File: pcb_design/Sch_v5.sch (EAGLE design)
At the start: 32 parts

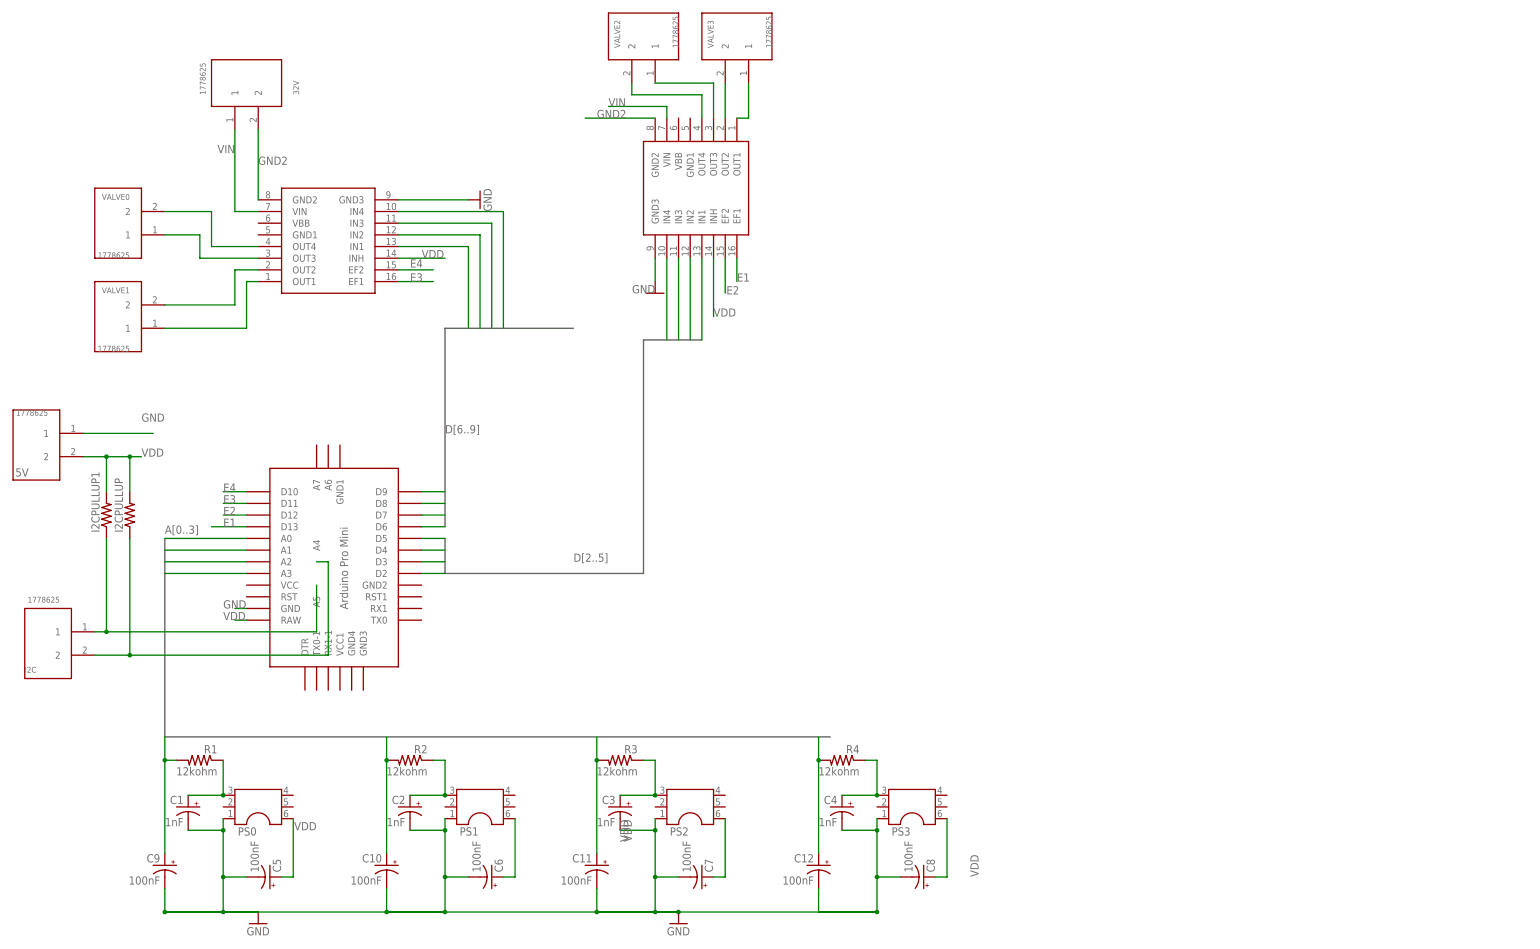
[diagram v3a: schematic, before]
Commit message: added byu parts library
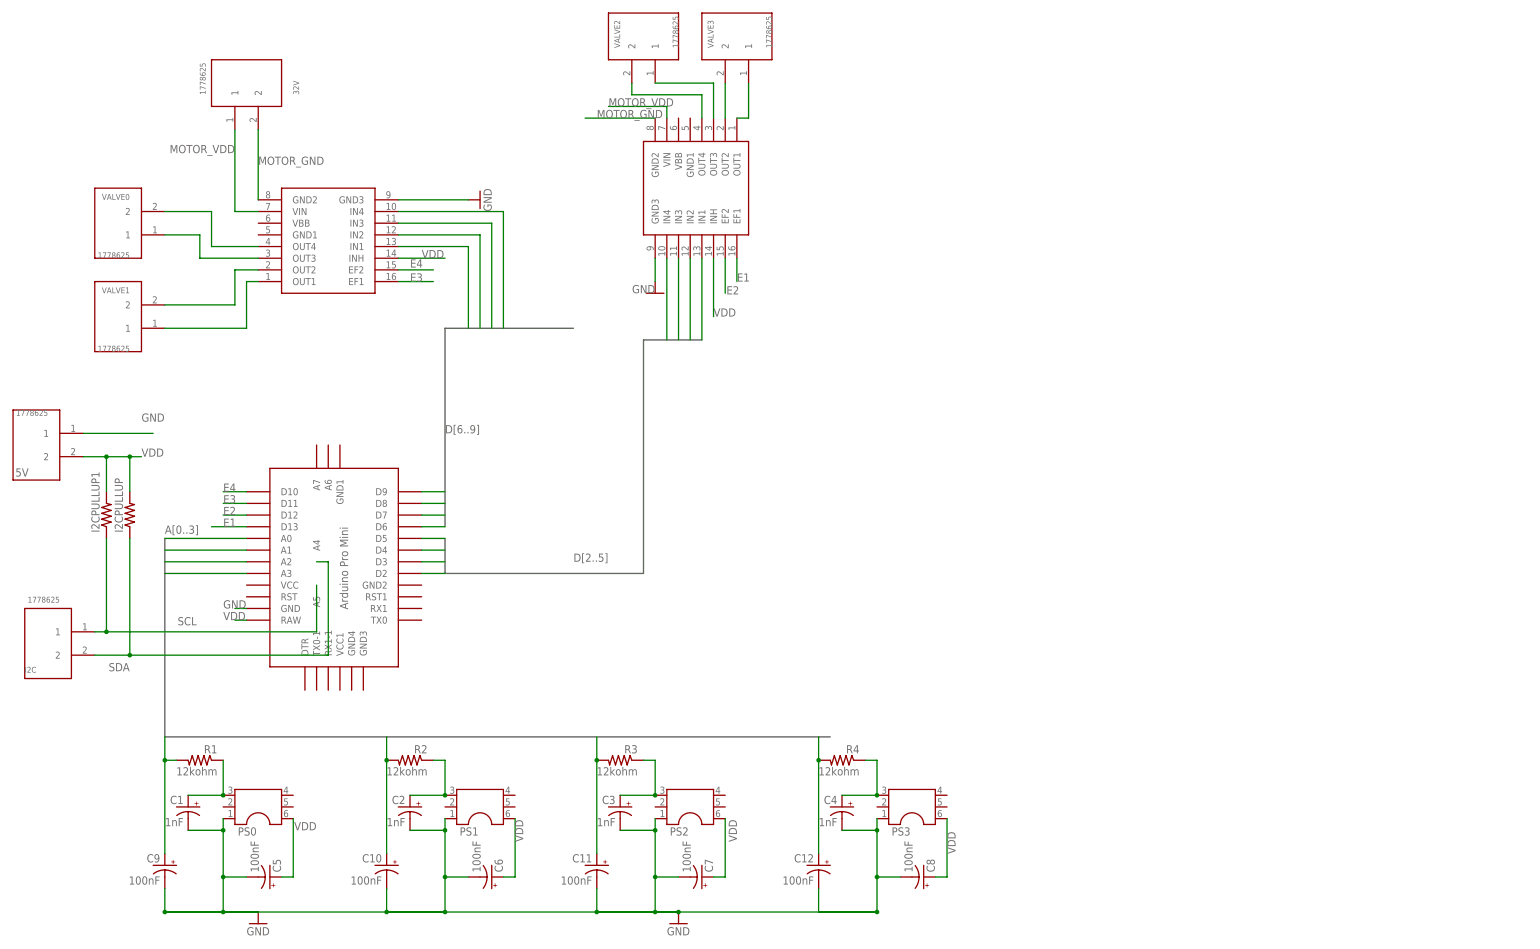
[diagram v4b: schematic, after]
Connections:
- net GND2 renamed MOTOR_GND
- net N$21 renamed SCL
- net N$9 renamed SDA
- net VIN renamed MOTOR_VDD
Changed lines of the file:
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@@
 <setting verticaltext="up"/>
 </settings>
-<grid distance="0.1" unitdist="inch" unit="inch" style="lines" multiple="1" display="no" altdistance="0.01" altunitdist="inch" altunit="inch"/>
+<grid distance="5" unitdist="mm" unit="mm" style="lines" multiple="1" display="no" altdistance="0.01" altunitdist="inch" altunit="inch"/>
 <layers>
 <layer number="1" name="Top" color="4" fill="1" visible="no" active="no"/>
@@
 </class>
 <class number="1" name="Power" width="0.3048" drill="0">
+<clearance class="1" value="0.508"/>
 </class>
-<class number="2" name="GND" width="0" drill="0">
+<class number="2" name="Motor Power" width="0.3048" drill="0">
+<clearance class="2" value="1.27"/>
 </class>
-<class number="3" name="Motor Power" width="0.3048" drill="0">
-<clearance class="3" value="0.0508"/>
+<class number="3" name="Analog Signal" width="0" drill="0">
+<clearance class="3" value="0.254"/>
+</class>
+<class number="4" name="I2C Bus" width="0" drill="0">
 </class>
 </classes>
@@
 </busses>
 <nets>
-<net name="GND" class="3">
+<net name="GND" class="0">
 <segment>
 <pinref part="GND4" gate="1" pin="GND"/>
@@
 <wire x1="58.42" y1="27.94" x2="58.42" y2="15.24" width="0.1524" layer="91"/>
 <wire x1="58.42" y1="15.24" x2="55.88" y2="15.24" width="0.1524" layer="91"/>
-<label x="81.28" y="22.86" size="1.778" layer="95" rot="MR90"/>
+<label x="58.42" y="22.86" size="1.778" layer="95" rot="MR90"/>
 </segment>
 <segment>
@@
 <wire x1="104.14" y1="27.94" x2="104.14" y2="15.24" width="0.1524" layer="91"/>
 <wire x1="104.14" y1="15.24" x2="101.6" y2="15.24" width="0.1524" layer="91"/>
-<label x="83.82" y="22.86" size="1.778" layer="95" rot="R90"/>
+<label x="106.68" y="22.86" size="1.778" layer="95" rot="R90"/>
 </segment>
 <segment>
@@
 <wire x1="152.4" y1="27.94" x2="152.4" y2="15.24" width="0.1524" layer="91"/>
 <wire x1="152.4" y1="15.24" x2="149.86" y2="15.24" width="0.1524" layer="91"/>
-<label x="157.48" y="15.24" size="1.778" layer="95" rot="MR90"/>
+<label x="152.48" y="20.24" size="1.778" layer="95" rot="MR90"/>
 </segment>
 <segment>
@@
 </segment>
 </net>
-<net name="VIN" class="3">
+<net name="MOTOR_VDD" class="2">
 <segment>
 <pinref part="U$3" gate="G$1" pin="VIN"/>
@@
 </segment>
 </net>
-<net name="GND2" class="0">
+<net name="MOTOR_GND" class="0">
 <segment>
 <pinref part="U$3" gate="G$1" pin="GND2"/>
@@
 </segment>
 </net>
-<net name="N$21" class="0">
+<net name="SCL" class="4">
 <segment>
 <pinref part="U$1" gate="G$1" pin="A5"/>
@@
 <junction x="-30.48" y="68.58"/>
 <pinref part="I2CPULLUP1" gate="G$1" pin="1"/>
+<label x="-15" y="70" size="1.778" layer="95"/>
 </segment>
 </net>
@@
 </segment>
 </net>
-<net name="A0" class="0">
+<net name="A0" class="3">
 <segment>
 <pinref part="U$1" gate="G$1" pin="A0"/>
@@
 </segment>
 </net>
-<net name="A1" class="0">
+<net name="A1" class="3">
 <segment>
 <pinref part="U$1" gate="G$1" pin="A1"/>
@@
 </segment>
 </net>
-<net name="A2" class="0">
+<net name="A2" class="3">
 <segment>
 <pinref part="U$1" gate="G$1" pin="A2"/>
@@
 </segment>
 </net>
-<net name="A3" class="0">
+<net name="A3" class="3">
 <segment>
 <pinref part="U$1" gate="G$1" pin="A3"/>
@@
 </segment>
 </net>
-<net name="N$9" class="0">
+<net name="SDA" class="4">
 <segment>
 <pinref part="I2C" gate="G$1" pin="2"/>
@@
 <junction x="-25.4" y="63.5"/>
 <pinref part="I2CPULLUP" gate="G$1" pin="1"/>
-</segment>
-</net>
+<label x="-30" y="60" size="1.778" layer="95"/>
+</segment>
+</net>

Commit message: commiting recent work
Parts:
- removed 32V, 5V, I2C: 1778625, 1778625:1778625
- removed I2CPULLUP, I2CPULLUP1: (no value), rcl:R-US_0204/7
- removed U$1: ABK-PRO-MINI, Arduino-clone:ABK-PRO-MINI
- removed U$2, U$3: A4990, pololu-stepper-driver:A4990
- added 12V_IN, I2C_IN, I2C_OUT: PHOENIX_CONNECTOR_1778625, byu_pressure_control:PHOENIX_CONNECTOR_1778625
- added DRIVER_A, DRIVER_B: A4990_DUAL_MOTOR_DRIVER_CARRIER, byu_pressure_control:A4990_DUAL_MOTOR_DRIVER_CARRIER
- added NANO: ARDUINO_NANO_EVERY, byu_pressure_control:ARDUINO_NANO_EVERY
- C1, C10, C11, C12, C2, C3, C4, C5, C6, C7, C8, C9: device rcl:CPOL-USE2.5-5 -> byu_pressure_control:CERAMIC_CAPACITOR
- PS0, PS1, PS2, PS3: value (none) -> PRESSURE_SENSOR_ABPDRNN100PGAA5; device RAD_2:ABPDRNN100PGAA5 -> byu_pressure_control:PRESSURE_SENSOR_ABPDRNN100PGAA5
- R1, R2, R3, R4: value 12kohm -> 12k
- VALVE0, VALVE1, VALVE2, VALVE3: value 1778625 -> PHOENIX_CONNECTOR_1778625; device 1778625:1778625 -> byu_pressure_control:PHOENIX_CONNECTOR_1778625
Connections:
- removed net E1: U$1.D13, U$3.EF1
- removed net E2: U$1.D12, U$3.EF2
- removed net E3: U$1.D11, U$2.EF1
- removed net E4: U$1.D10, U$2.EF2
- removed net MOTOR_VDD: 32V.1, U$2.VIN, U$3.VIN
- removed net N$13: U$3.OUT1, VALVE3.1
- removed net N$14: U$3.OUT2, VALVE3.2
- removed net N$15: U$3.OUT3, VALVE2.1
- removed net N$16: U$3.OUT4, VALVE2.2
- removed net VDD: 5V.2, C5.+, C6.+, C7.+, C8.+, I2CPULLUP.2, I2CPULLUP1.2, PS0.6, PS1.6, PS2.6, PS3.6, U$1.RAW, U$2.INH, U$3.INH
- new net 12V: 12V_IN.1, DRIVER_A.VIN, DRIVER_B.VIN, NANO.VIN
- new net 5V: C5.2, C6.2, C7.2, C8.2, DRIVER_A.INH, DRIVER_B.INH, NANO.5V, PS0.VSUPPLY, PS1.VSUPPLY, PS2.VSUPPLY, PS3.VSUPPLY
- new net EF1_A: DRIVER_A.EF1, NANO.D10
- new net EF1_B: DRIVER_B.EF1, NANO.D12
- new net EF2_A: DRIVER_A.EF2, NANO.D11
- new net EF2_B: DRIVER_B.EF2, NANO.A7
- new net N$10: DRIVER_B.OUT2, VALVE3.2
- new net N$11: DRIVER_B.OUT3, VALVE2.1
- new net N$12: DRIVER_B.OUT4, VALVE2.2
- new net N$9: DRIVER_B.OUT1, VALVE3.1
- net A0: now also C9.1, NANO.A0; no longer C9.+, U$1.A0
- net A1: now also C10.1, NANO.A1; no longer C10.+, U$1.A1
- net A2: now also C11.1, NANO.A2; no longer C11.+, U$1.A2
- net A3: now also C12.1, NANO.A3; no longer C12.+, U$1.A3
- net D2: now also DRIVER_B.IN1, NANO.D2; no longer U$1.D2, U$3.IN1
- net D3: now also DRIVER_B.IN2, NANO.D3; no longer U$1.D3, U$3.IN2
- net D4: now also DRIVER_B.IN3, NANO.D4; no longer U$1.D4, U$3.IN3
- net D5: now also DRIVER_B.IN4, NANO.D5; no longer U$1.D5, U$3.IN4
- net D6: now also DRIVER_A.IN1, NANO.D6; no longer U$1.D6, U$2.IN1
- net D7: now also DRIVER_A.IN2, NANO.D7; no longer U$1.D7, U$2.IN2
- net D8: now also DRIVER_A.IN3, NANO.D8; no longer U$1.D8, U$2.IN3
- net D9: now also DRIVER_A.IN4, NANO.D9; no longer U$1.D9, U$2.IN4
- net GND: now also C1.2, C10.2, C11.2, C12.2, C2.2, C3.2, C4.2, C5.1, C6.1, C7.1, C8.1, C9.2, DRIVER_A.GND, DRIVER_B.GND, NANO.GND, PS0.GND, PS1.GND, PS2.GND, PS3.GND; no longer 5V.1, C1.-, C10.-, C11.-, C12.-, C2.-, C3.-, C4.-, C5.-, C6.-, C7.-, C8.-, C9.-, PS0.1, PS1.1, PS2.1, PS3.1, U$1.GND, U$2.GND3, U$3.GND3
- net MOTOR_GND: now also 12V_IN.2, DRIVER_A.MTR_GND, DRIVER_B.MTR_GND; no longer 32V.2, U$2.GND2, U$3.GND2
- net N$1: now also C1.1, PS0.VOUT; no longer C1.+, PS0.3
- net N$2: now also C2.1, PS1.VOUT; no longer C2.+, PS1.3
- net N$3: now also C3.1, PS2.VOUT; no longer C3.+, PS2.3
- net N$4: now also C4.1, PS3.VOUT; no longer C4.+, PS3.3
- net N$5: now also DRIVER_A.OUT2; no longer U$2.OUT2
- net N$6: now also DRIVER_A.OUT1; no longer U$2.OUT1
- net N$7: now also DRIVER_A.OUT3; no longer U$2.OUT3
- net N$8: now also DRIVER_A.OUT4; no longer U$2.OUT4
- net SCL: now also I2C_IN.1, I2C_OUT.1, NANO.A5/SCL; no longer I2C.1, I2CPULLUP1.1, U$1.A5
- net SDA: now also I2C_IN.2, I2C_OUT.2, NANO.A4/SDA; no longer I2C.2, I2CPULLUP.1, U$1.A4
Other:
- note added: "NOTE: There are 2 grounds that are NOT connected to each other. This was done in an attempt to decrease noise in the analog sensor GND. The MOTOR_GND is the botom copper pour and GND is the top copper pour. By only connecting these grounds through the driver boards, this allows the small noisy currents on MOTOR_GND a lower impedance path back to the power source."
- note removed: "5V"
- moved on the sheet: R1, R2, R3, R4, VALVE0, VALVE1, VALVE2, VALVE3

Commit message: final version of pcb I think
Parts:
- renumbered NANO to NANO1
